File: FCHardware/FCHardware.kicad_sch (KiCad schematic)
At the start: 15 parts, among them U1 ESC_Xrotor_65A_4in1, U4 TPS629203, U5 MPU-6050

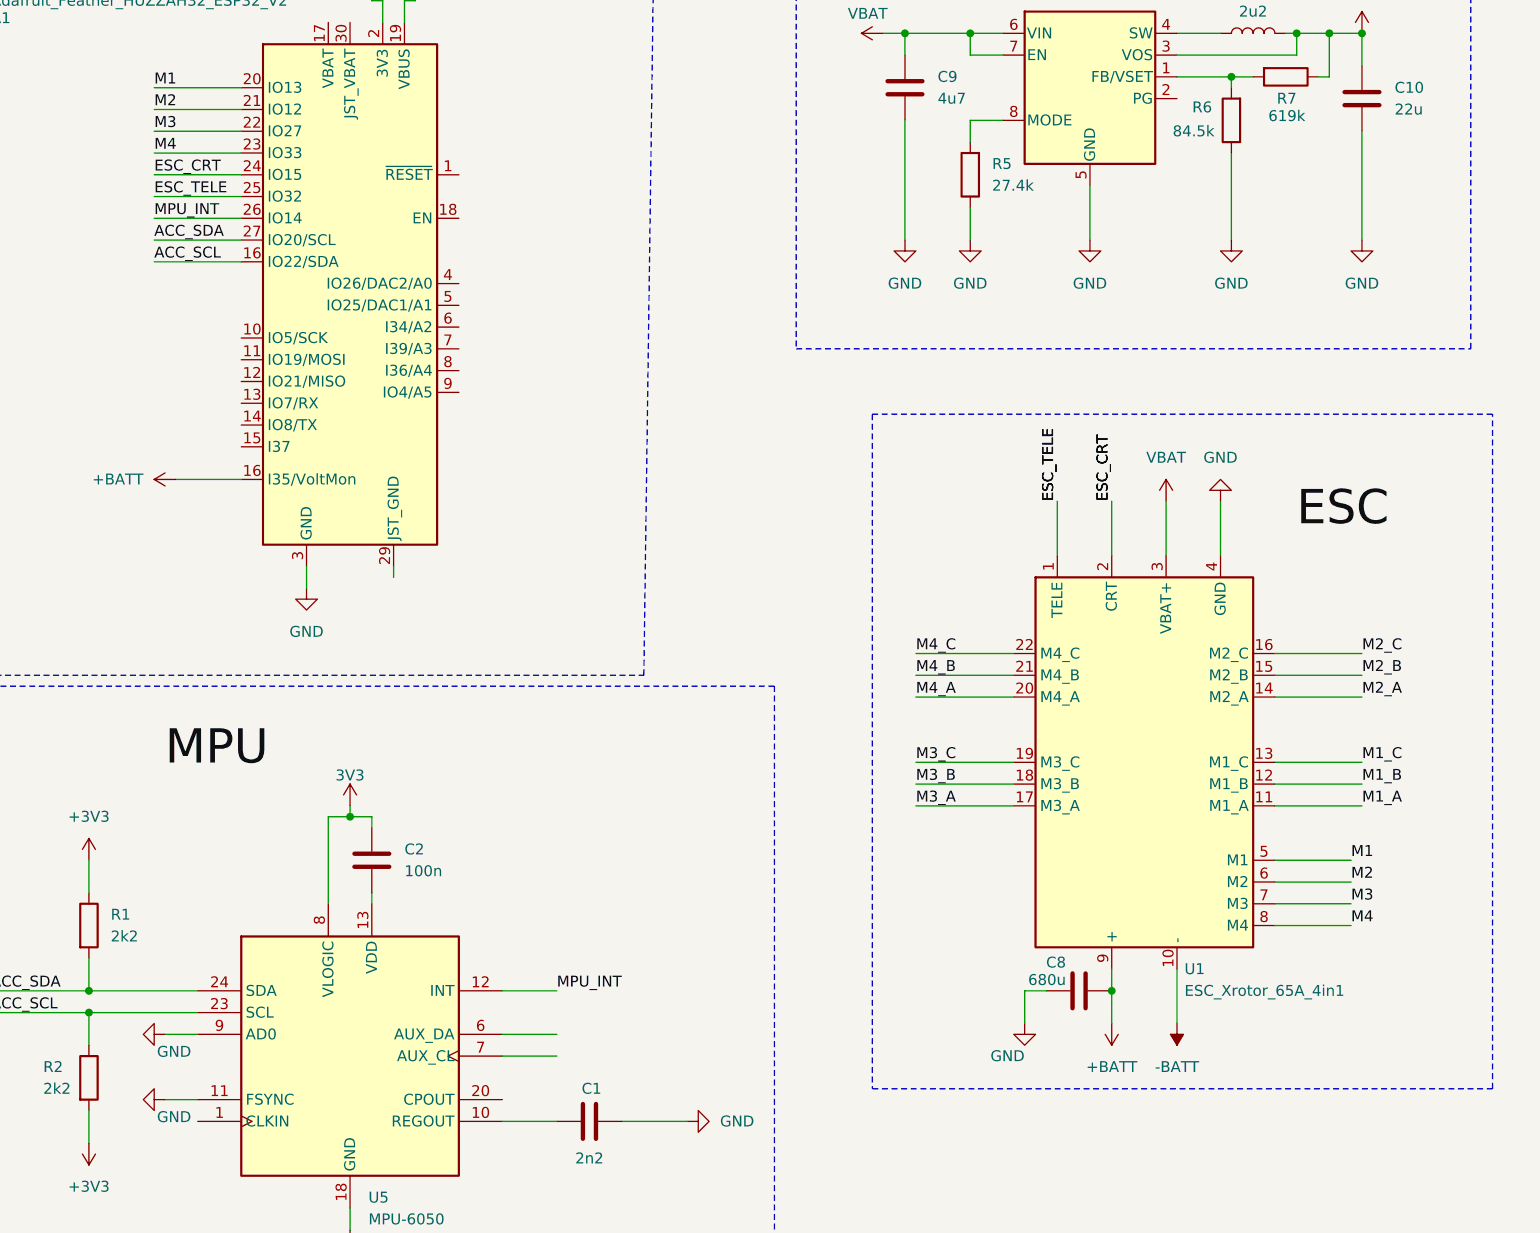
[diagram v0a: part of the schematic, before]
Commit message: Added voltage monitor
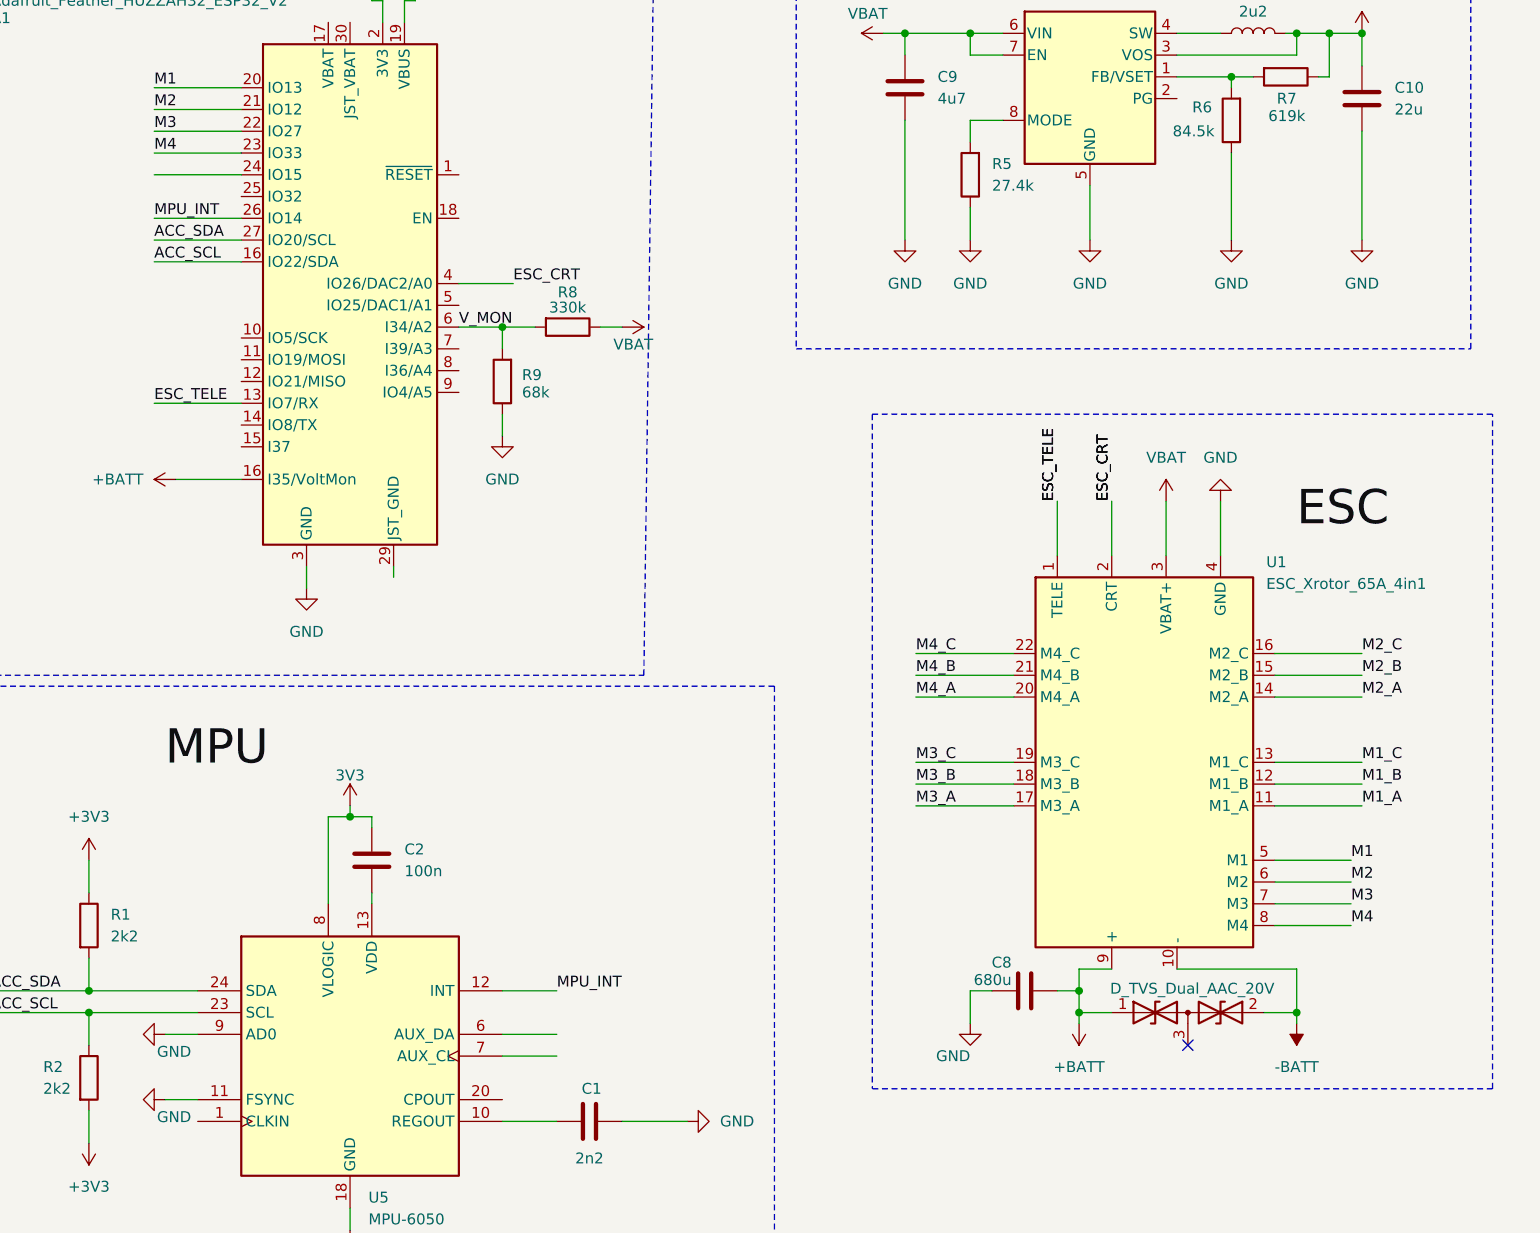
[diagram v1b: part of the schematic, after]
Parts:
- added D1: D_TVS_Dual_AAC_20V, symbol Device:D_TVS_Dual_AAC
- added R8: 330k, symbol Device:R
- added R9: 68k, symbol Device:R
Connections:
- net +BATT: now also D1.1 (A1)
- net -BATT: now also D1.2 (A2)
- net ESC_CRT: now also A1.4 (IO26/DAC2/A0); no longer A1.24 (IO15)
- net ESC_TELE: now also A1.13 (IO7/RX); no longer A1.25 (IO32)
- net GND: now also R9.1
- net VBAT: now also R8.1
- net V_MON: now reaches A1.6 (I34/A2)
- net V_MON: now also R8.2, R9.2
- no-connect marks 0 -> 1
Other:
- moved on the sheet: C8

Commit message: Updated documentation
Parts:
- added C11: 100n, symbol Device:C
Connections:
- net +5V: now also C11.1
- net +BATT: no longer C8.2
- net -BATT: now also C8.2
- net GND: now also D1.3 (common), C11.2
- no-connect marks 1 -> 0
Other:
- moved on the sheet: C1, C2, C8, R1, R2, U1, U5

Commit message: Switched to ESP32-S3-MINI-1U
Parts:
- added C3: 100n, symbol Device:C
- added Q1: BUT11, Package_TO_SOT_THT:TO-220-3_Vertical, symbol Transistor_BJT:BUT11
- added R10: 68k, symbol Device:R
- added R11: 330k, symbol Device:R
- added R12, R13: 10k, symbol Device:R
- added U2: ESP32-S3-MINI-1U, RF_Module:ESP32-S2-MINI-1U, symbol RF_Module:ESP32-S3-MINI-1U
- R6: value 84.5k -> 137k
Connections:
- net +3V3: now also C10.1, L2.2, R7.1, U4.3 (VOS), Q1.2 (C), R12.2, U2.3 (3V3)
- net +5V: no longer C10.1, L2.2, R7.1, U4.3 (VOS)
- net ACC_SCL: now also U2.13 (IO9)
- net ACC_SDA: now also U2.12 (IO8)
- net ESC_CRT: now also U2.37 (IO41)
- net ESC_TELE: now also U2.40 (RXD0)
- net GND: now also C3.1, Q1.3 (E), R10.2, U2.1 (GND), U2.2 (GND), U2.42 (GND), U2.43 (GND), U2.46 (GND), U2.47 (GND), U2.48 (GND), U2.49 (GND), U2.50 (GND), U2.51 (GND), U2.52 (GND), U2.53 (GND), U2.54 (GND), U2.55 (GND), U2.56 (GND), U2.57 (GND), U2.58 (GND), U2.59 (GND), U2.60 (GND), U2.61 (GND), U2.62 (GND), U2.63 (GND), U2.64 (GND), U2.65 (GND)
- net M1: now also U2.25 (IO21)
- net M2: now also U2.28 (IO33)
- net M3: now also U2.31 (IO35)
- net M4: now also U2.33 (IO37)
- net MPU_INT: now also U2.35 (IO39)
- net VBAT: now also R11.1
- net V_MON: now also R10.1, R11.2, U2.7 (IO3)
- new net: C3.2, R12.1, U2.45 (EN)
- new net: Q1.1 (B), R13.2
- new net BOOT: R13.1, U2.4 (IO0)

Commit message: Final fixes before updating to 6S
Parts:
- removed A1: Adafruit_Feather_HUZZAH32_ESP32_V2, Module:Adafruit_Feather, symbol Custom_ESP32_Library:Adafruit_Feather_HUZZAH32_ESP32_v2
- removed C11: 100n, symbol Device:C
- removed Q1: BUT11, Package_TO_SOT_THT:TO-220-3_Vertical, symbol Transistor_BJT:BUT11
- removed R8: 330k, symbol Device:R
- removed R9: 68k, symbol Device:R
- added C4, C5: 5k1, symbol Device:C
- added C6: 100n, symbol Device:C
- added H1, H2, H3, H4: MountingHole, symbol Mechanical:MountingHole
- added J2: USB_C_Receptacle_USB2.0_16P, symbol Connector:USB_C_Receptacle_USB2.0_16P
- added R14, R15: 22, symbol Device:R
- added R16, R17: 5k1 +-5%, symbol Device:R
- added SW1: SW_Push, symbol Switch:SW_Push
- added TP1: GNDTestPoint, symbol Connector:TestPoint
- added TP2: VBATTestPoint, symbol Connector:TestPoint
- added TP3: 3V3TestPoint, symbol Connector:TestPoint
- added TP4: ENTestPoint, symbol Connector:TestPoint
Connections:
- net +3V3: now also R13.1, C6.2, TP3.1; no longer U2.3 (3V3)
- net BOOT: now also R13.2, SW1.2; no longer R13.1
- net ESC_CRT: now also U2.38 (IO42); no longer U2.37 (IO41)
- net GND: now also C4.2, C5.2, J2.A1 (GND), J2.A12 (GND), J2.B1 (GND), J2.B12 (GND), J2.S1 (SHIELD), R16.1, R17.2, SW1.1, TP1.1, TP4.1
- net M1: now also U2.26 (IO26); no longer U2.25 (IO21)
- net M2: now also U2.29 (IO34); no longer U2.28 (IO33)
- net M3: now also U2.32 (IO36); no longer U2.31 (IO35)
- net M4: now also U2.34 (IO38); no longer U2.33 (IO37)
- net MPU_INT: now also U2.36 (IO40); no longer U2.35 (IO39)
- net VBAT: now also TP2.1
- net at U2.23 (USB_D-): now also R14.2
- net at U2.24 (USB_D+): now also R15.1
- new net: C6.1, U2.3 (3V3)
- new net: J2.B5 (CC2), R17.1
- new net: J2.A5 (CC1), R16.2
- new net INP_+5V: J2.A4 (VBUS), J2.A9 (VBUS), J2.B4 (VBUS), J2.B9 (VBUS)
- new net USB_D+: C5.1, J2.A6 (D+), R15.2
- new net USB_D-: C4.1, J2.A7 (D-), R14.1
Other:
- moved on the sheet: C1, C10, C2, C3, C8, C9, L2, R1, R10, R11, R12, R13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

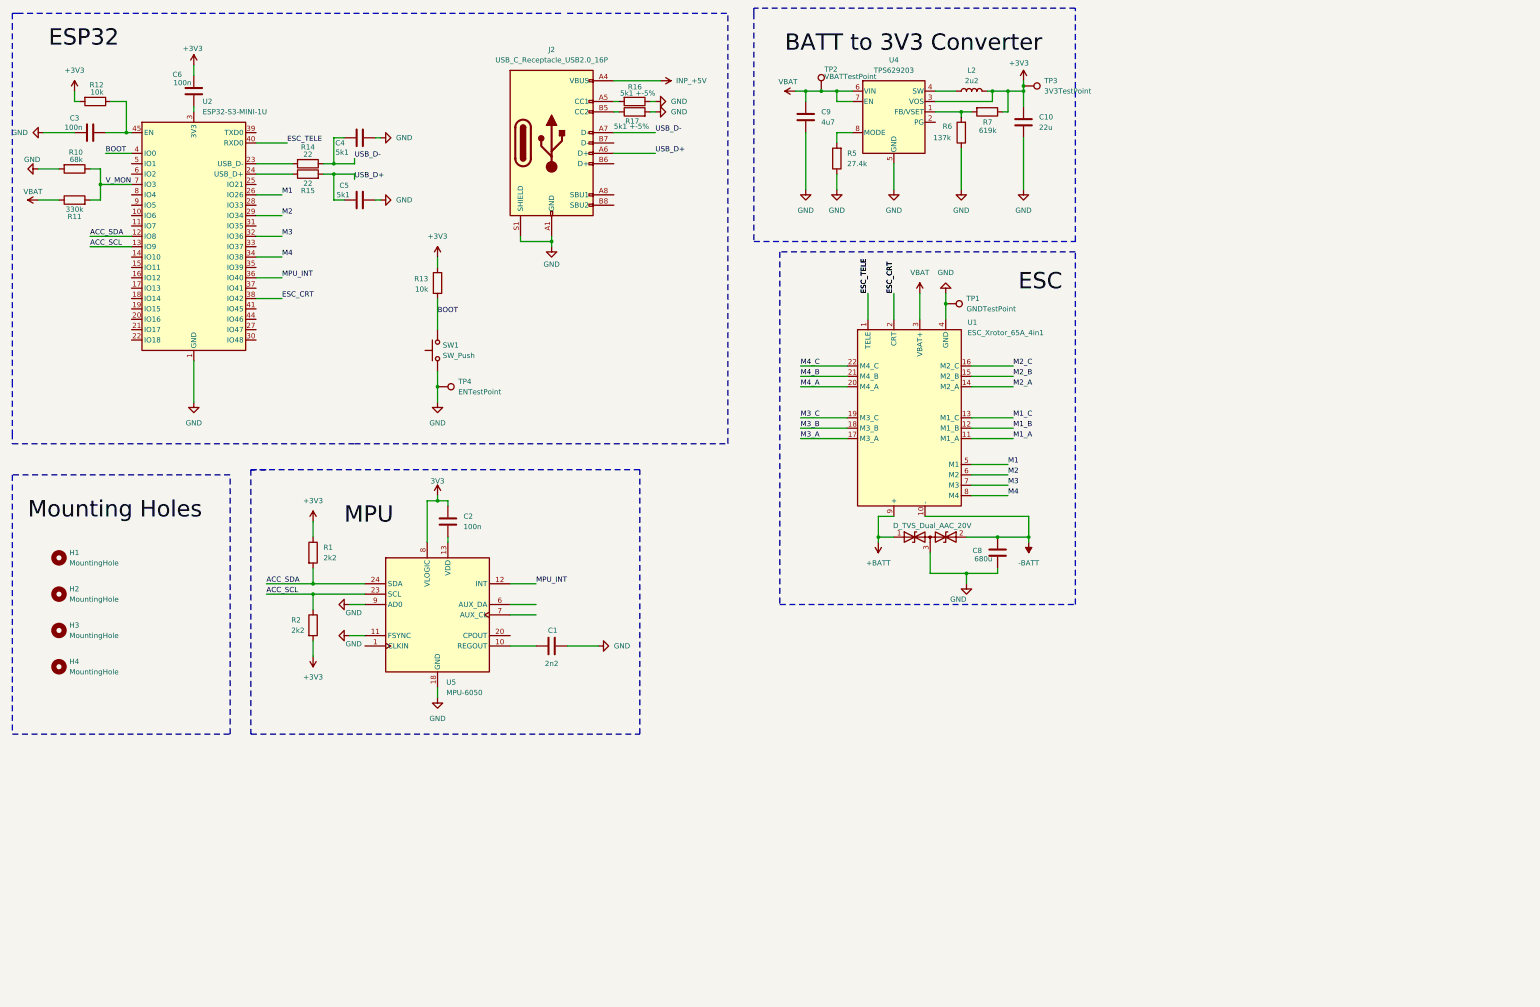
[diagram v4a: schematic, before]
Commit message: Added TPSM63603 and wired it starting the transition towards the 4S - 6S architecture
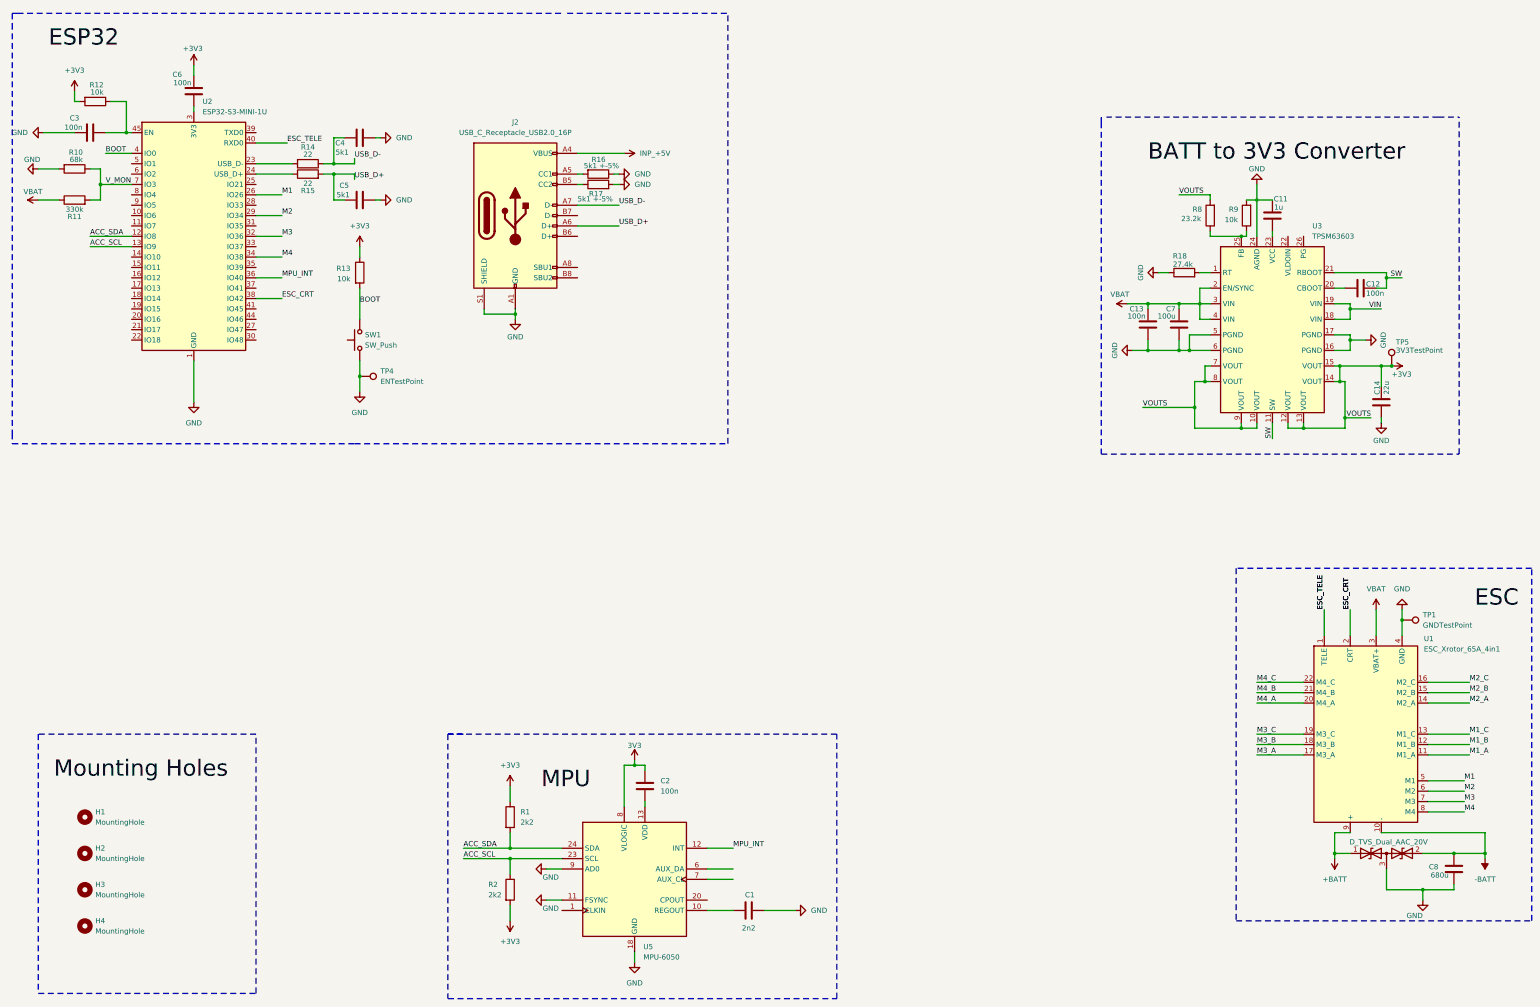
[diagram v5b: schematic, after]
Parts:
- removed C10: 22u, symbol Device:C
- removed C9: 4u7, symbol Device:C
- removed L2: 2u2, symbol Device:L
- removed R5: 27.4k, symbol Device:R
- removed R6: 137k, symbol Device:R
- removed R7: 619k, symbol Device:R
- removed TP2: VBATTestPoint, symbol Connector:TestPoint
- removed TP3: 3V3TestPoint, symbol Connector:TestPoint
- removed U4: TPS629203, Package_SON:WSON-8-1EP_2x2mm_P0.5mm_EP0.9x1.6mm_ThermalVias, symbol CustomSymbols:TPS629203
- added C11: 1u, symbol Device:C
- added C12, C13: 100n, symbol Device:C
- added C14: 22u, symbol Device:C
- added C7: 100u, symbol Device:C
- added R18: 27.4k, symbol Device:R
- added R8: 23.2k, symbol Device:R
- added R9: 10k, symbol Device:R
- added TP5: 3V3TestPoint, symbol Connector:TestPoint
- added U3: TPSM63603, RF_Module:ESP32-C3-WROOM-02, symbol CustomSymbols:TPSM63603
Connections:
- net +3V3: now also C14.1, R8.2, TP5.1, U3.10 (VOUT), U3.12 (VOUT), U3.13 (VOUT), U3.14 (VOUT), U3.15 (VOUT), U3.7 (VOUT), U3.8 (VOUT), U3.9 (VOUT)
- net GND: now also C11.1, C13.2, C14.2, C7.2, R18.1, R9.2, U3.16 (PGND), U3.17 (PGND), U3.24 (AGND), U3.5 (PGND), U3.6 (PGND)
- net VBAT: now also C13.1, C7.1, U3.2 (EN/SYNC), U3.3 (VIN), U3.4 (VIN)
- new net: C11.2, U3.23 (VCC)
- new net: R8.1, R9.1, U3.25 (FB)
- new net: R18.2, U3.1 (RT)
- new net: C12.2, U3.20 (CBOOT)
- new net SW: C12.1, U3.11 (SW), U3.21 (RBOOT)
- new net VIN: U3.18 (VIN), U3.19 (VIN)
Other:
- moved on the sheet: C1, C2, C8, H1, H2, H3, H4, J2, R1, R13, R16, R17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

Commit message: Replaced wrong diodes, added smoothening capacitorsr
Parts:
- removed D1: D_TVS_Dual_AAC_20V, symbol Device:D_TVS_Dual_AAC
- added C10, C9: 100n, symbol Device:C
- added C15: 10u, symbol Device:C
- added D2: SMBJ28A, symbol Device:D
- added U4: USBLC6-2SC6, Package_TO_SOT_SMD:SOT-23-6, symbol Power_Protection:USBLC6-2SC6
- C2: value 100n -> 1u
- R11: value 330k -> 510k
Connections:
- net +3V3: now also C1.2, C11.1, C13.2, C14.2, C3.1, C4.2, C5.2, C6.1, C7.2, J2.A1 (GND), J2.A12 (GND), J2.B1 (GND), J2.B12 (GND), J2.S1 (SHIELD), R16.1, R17.2, R18.1, R9.2, SW1.1, TP1.1, TP4.1, U1.4 (GND), U2.1 (GND), U2.2 (GND), U2.3 (3V3), U2.42 (GND), U2.43 (GND), U2.46 (GND), U2.47 (GND), U2.48 (GND), U2.49 (GND), U2.50 (GND), U2.51 (GND), U2.52 (GND), U2.53 (GND), U2.54 (GND), U2.55 (GND), U2.56 (GND), U2.57 (GND), U2.58 (GND), U2.59 (GND), U2.60 (GND), U2.61 (GND), U2.62 (GND), U2.63 (GND), U2.64 (GND), U2.65 (GND), U3.16 (PGND), U3.17 (PGND), U3.24 (AGND), U3.5 (PGND), U3.6 (PGND), U5.11 (FSYNC), U5.18 (GND), U5.9 (AD0), C15.1, C15.2, C9.1, U4.2 (GND)
- net +BATT: now also D2.2 (A)
- net -BATT: now also C8.1, D2.1 (K)
- net INP_+5V: now also U4.5 (VBUS)
- net USB_D+: now also U4.3 (I/O2), U4.4 (I/O2)
- net USB_D-: now also U4.1 (I/O1), U4.6 (I/O1)
- net V_MON: now also U2.8 (IO4); no longer U2.7 (IO3)
- net at U5.13 (VDD): now also C10.1; no longer C2.1
- removed net GND: C1.2, C11.1, C13.2, C14.2, C3.1, C4.2, C5.2, C7.2, C8.1, J2.A1 (GND), J2.A12 (GND), J2.B1 (GND), J2.B12 (GND), J2.S1 (SHIELD), R10.2, R16.1, R17.2, R18.1, R9.2, SW1.1, TP1.1, TP4.1, U1.4 (GND), U2.1 (GND), U2.2 (GND), U2.42 (GND), U2.43 (GND), U2.46 (GND), U2.47 (GND), U2.48 (GND), U2.49 (GND), U2.50 (GND), U2.51 (GND), U2.52 (GND), U2.53 (GND), U2.54 (GND), U2.55 (GND), U2.56 (GND), U2.57 (GND), U2.58 (GND), U2.59 (GND), U2.60 (GND), U2.61 (GND), U2.62 (GND), U2.63 (GND), U2.64 (GND), U2.65 (GND), U3.16 (PGND), U3.17 (PGND), U3.24 (AGND), U3.5 (PGND), U3.6 (PGND), U5.11 (FSYNC), U5.18 (GND), U5.9 (AD0)
- new net: C10.2, C2.1
- new net: C9.2, R10.2
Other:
- moved on the sheet: C1, C11, C12, C13, C14, C2, C3, C4, C5, C6, C7, C8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
